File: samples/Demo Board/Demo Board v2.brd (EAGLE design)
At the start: 88.9 x 50.8 mm, 145 parts

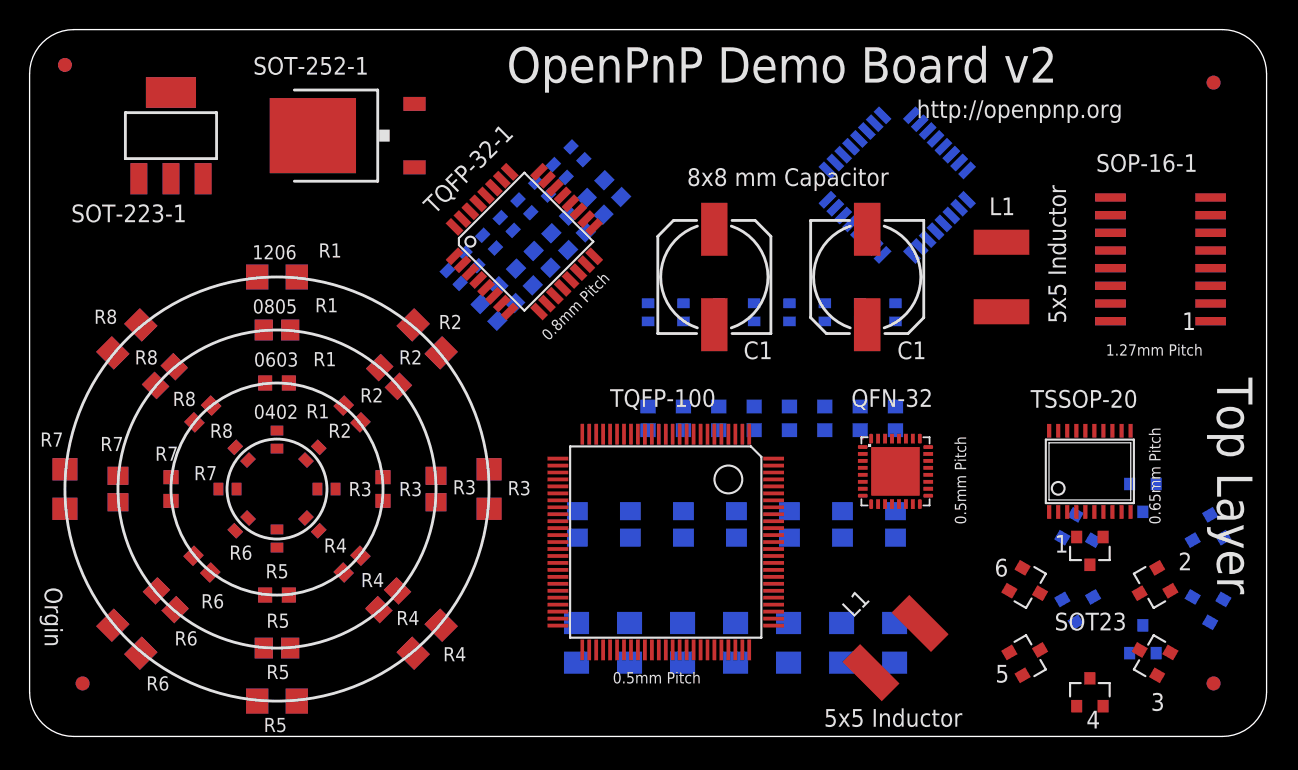
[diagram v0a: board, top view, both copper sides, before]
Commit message: Added coverage for all major IC pitch types. 1mm keepout around all fiducials. Bottom layer tests. Logical placement and labeling for top and bottom layers. Tricky/tall/heavy components (capacitors, inductors). Calibration ruler on bottom layer.
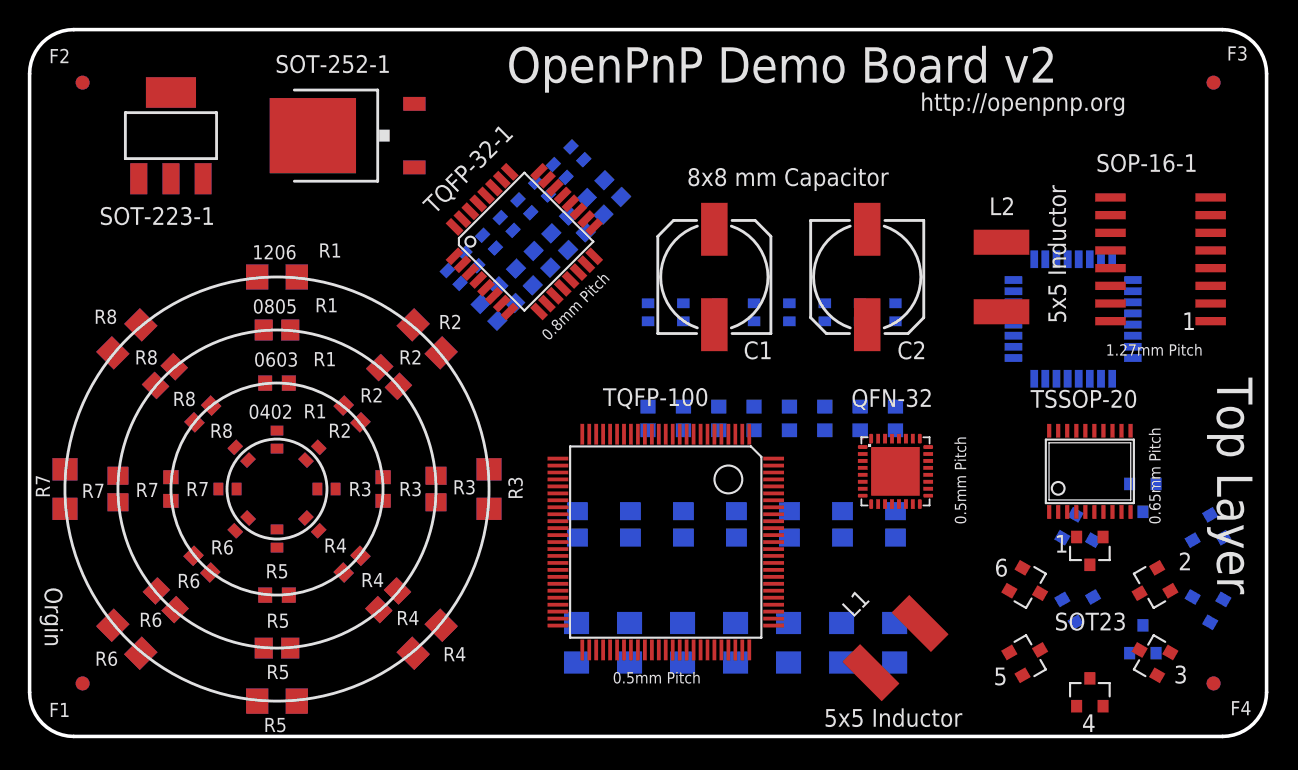
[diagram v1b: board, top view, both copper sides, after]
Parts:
- removed FID-9: (no value), adafruit:FIDUCIAL_1MM
- removed SOP-16-2: (no value), ref-packages:SOP16
- added FID-8: (no value), adafruit:FIDUCIAL_1MM
- moved FID-6 92.0 mm to (3.81, 47.0), flipped to the bottom
- moved FID-3 82.6 mm to (85.1, 47.0)
- moved FID-2 81.3 mm to (3.81, 47.0)
- moved FID-5 44.5 mm to (3.81, 3.81)
- moved TQFP-32-2 15.9 mm to (75.0, 30.0), turned to 0 degrees
- flipped FID-4 to the top
- renumbered FID-14 to FID-7, TQFP-1 to TQFP-32-1
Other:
- board text added: "10x10mm"
- board text added: "1mm Ruler"
- board text added: "C2"
- board text added: "F1"
- board text added: "F2"
- board text added: "F3"
- board text added: "F4"
- board text added: "F5"
- board text added: "F6"
- board text added: "F7"
- board text added: "F8"
- board text added: "L2"
- board text removed: "Bottom Layer"
- board text removed: "SOP-16-2"

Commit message: Add lines to ruler for clarity and to aid in measuring image distortion
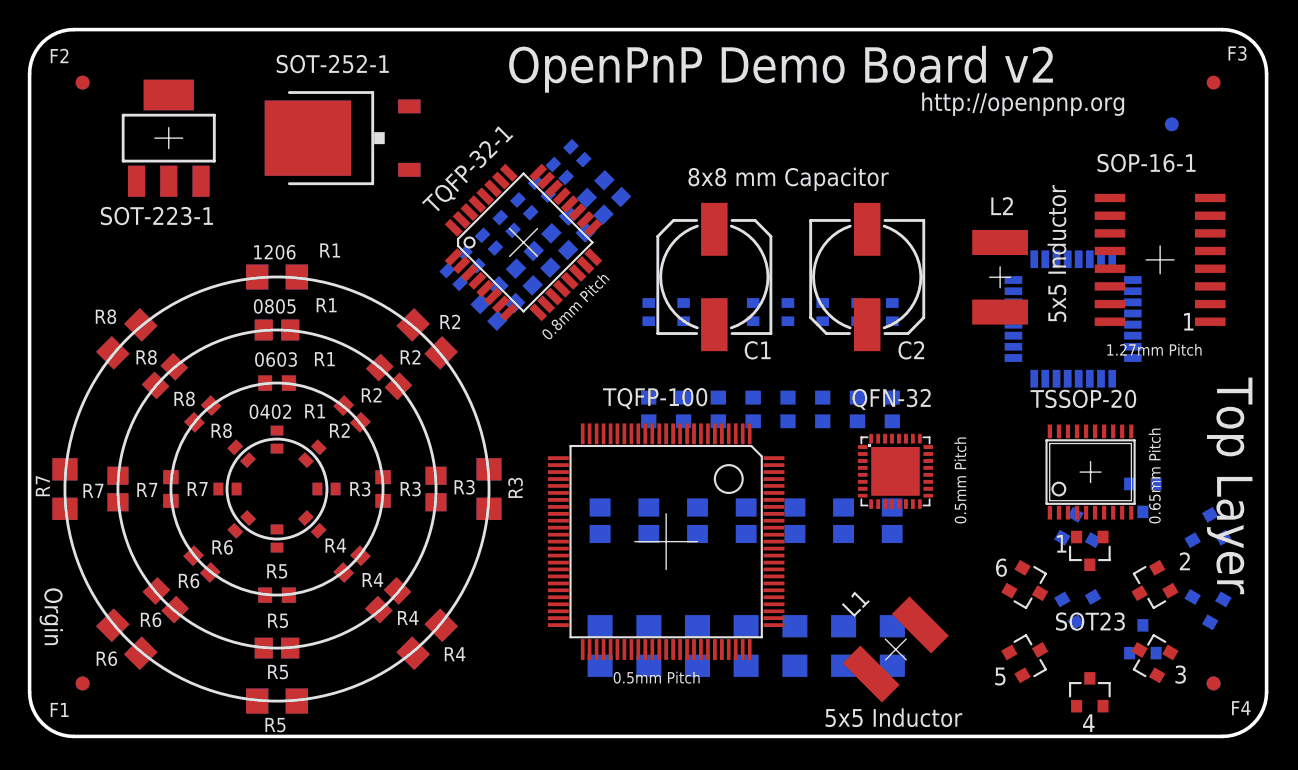
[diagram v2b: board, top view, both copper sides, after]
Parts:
- moved FID-7 4.24 mm to (82.1, 44.0)
- moved R1206-17 1.71 mm to (41.0, 6.50)
- moved R0805-17 1.65 mm to (41.0, 15.5)
- moved R1206-18 1.40 mm to (44.5, 6.50)
- moved R0805-18 1.35 mm to (44.5, 15.5)
- moved R1206-19 1.10 mm to (48.0, 6.50)
- moved R0805-19 1.04 mm to (48.0, 15.5)
- moved R1206-20 0.80 mm to (51.5, 6.50)
- moved R0805-20 0.75 mm to (51.5, 15.5)
- moved R0603-32 0.68 mm to (62.0, 23.5)
- moved R0603-31 0.67 mm to (59.5, 23.5)
- moved R0603-30 0.66 mm to (57.0, 23.5)
- moved R0603-29 0.65 mm to (54.5, 23.5)
- moved R0603-28 0.64 mm to (52.0, 23.5)
- moved R0603-25 0.64 mm to (44.5, 23.5)
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
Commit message: Changed ruler to copper Added .5mm spacing to ruler Added ruler to Top Layer so now it is on top and bottom Added 0201 components. Created new components named BOTTOM_RULER_ORIGIN and TOP_RULER_ORIGIN. Now they will show up in job list so you can zoom to them.
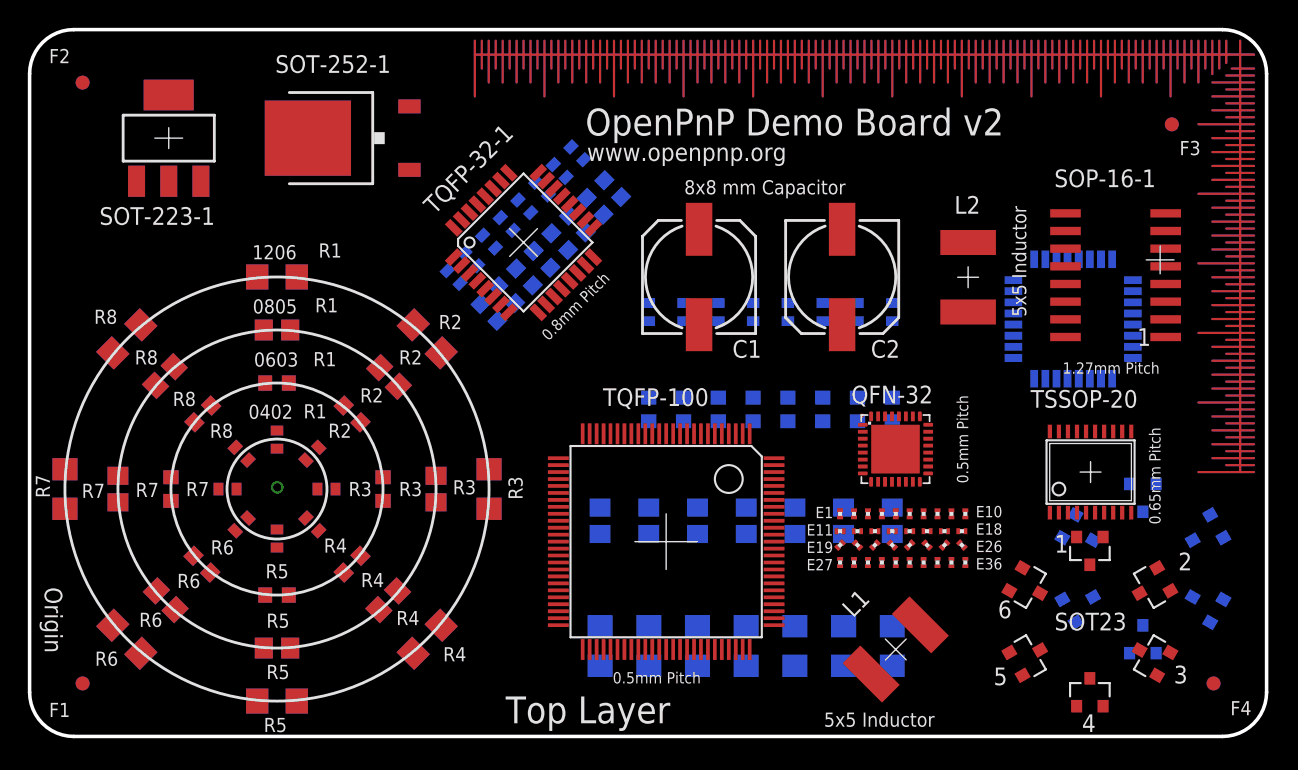
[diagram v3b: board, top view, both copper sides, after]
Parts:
- added BOTTOM_RULER_ORGIN, BOTTOM_RULER_ORGIN1: (no value), ref-packages:REFERENCE_BOTTOM
- added E$12, E$13, E$14, E$15, E$16, E$17, E$19, E$2, E$20, E$21, E$22, E$23, E$24, E$25, E$26, E$28, E$29, E$3, E$30, E$31, E$32, E$33, E$34, E$35, E$4, E$5, E$6, E$7, E$8, E$9, E1, E10, E11, E18, E27, E36: (no value), rcl:R0201
- moved FID-3 4.24 mm to (82.1, 44.0)
- moved SOP-16-1 3.38 mm to (78.0, 33.1)
- moved L2 2.30 mm to (67.5, 33.0)
- moved C2 1.80 mm to (58.4, 33.0)
- moved QFN-32 1.60 mm to (62.2, 20.6)
- moved C1 1.10 mm to (48.1, 33.0)
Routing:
- net S$1: track 0.00 -> 60.0 mm
- net S$288: track 0.00 -> 55.9 mm
- net S$240: track 0.00 -> 35.0 mm
- net S$78: track 0.00 -> 34.9 mm
- net S$98: track 0.00 -> 6.00 mm
- net S$97: track 0.00 -> 6.00 mm
- net S$91: track 0.00 -> 6.00 mm
- net S$90: track 0.00 -> 6.00 mm
- net S$84: track 0.00 -> 6.00 mm
- net S$83: track 0.00 -> 6.00 mm
- net S$70: track 0.00 -> 6.00 mm
- net S$69: track 0.00 -> 6.00 mm
- net S$63: track 0.00 -> 6.00 mm
- net S$62: track 0.00 -> 6.00 mm
- net S$6: track 0.00 -> 6.00 mm
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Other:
- board text added: "0.5, 1, 5, 10 mm"
- board text added: "E1"
- board text added: "E10"
- board text added: "E11"
- board text added: "E18"
- board text added: "E19"
- board text added: "E26"
- board text added: "E27"
- board text added: "E36"
- board text added: "Origin"
- board text added: "Ruler Spacing"
- board text added: "www.openpnp.org"
- board text removed: "1mm Ruler"
- board text removed: "Orgin"
- board text removed: "http://openpnp.org"

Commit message: Changing the sample to the version i physically have
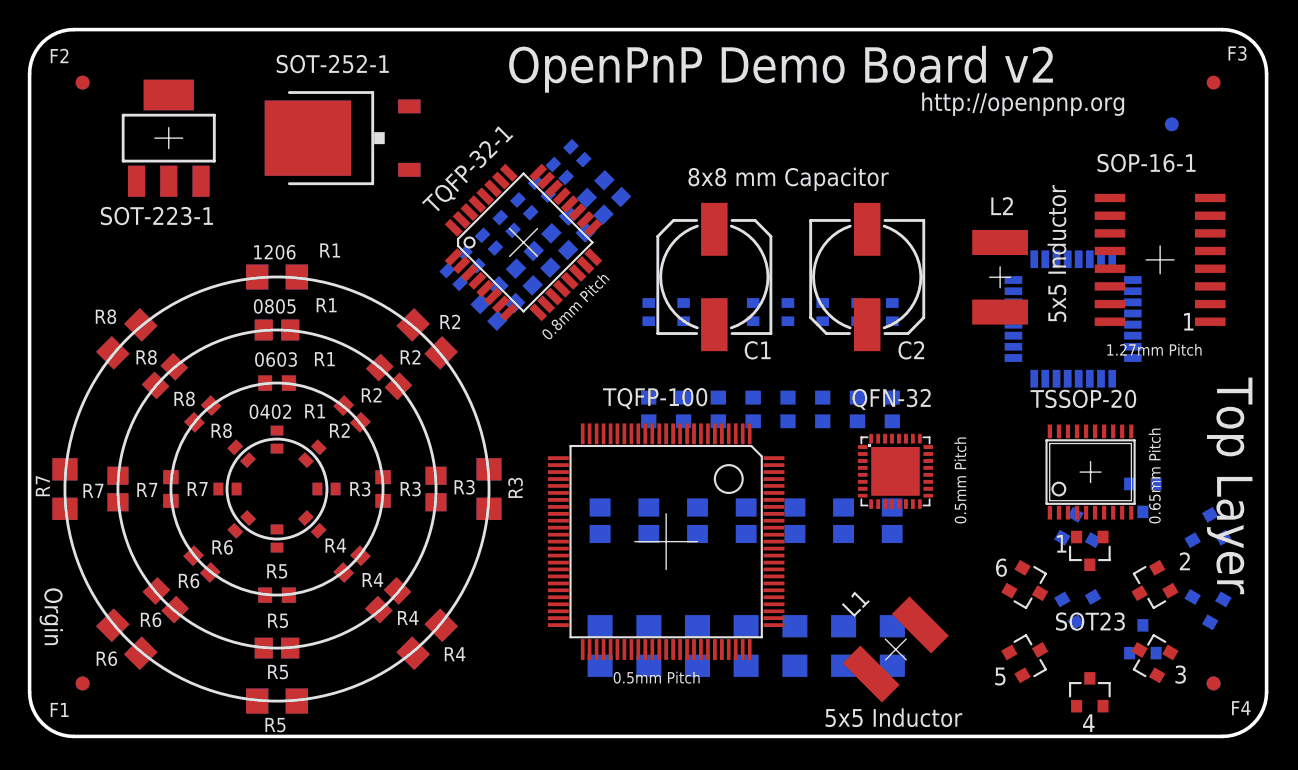
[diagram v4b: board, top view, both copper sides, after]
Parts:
- removed BOTTOM_RULER_ORGIN, BOTTOM_RULER_ORGIN1: (no value), ref-packages:REFERENCE_BOTTOM
- removed E$12, E$13, E$14, E$15, E$16, E$17, E$19, E$2, E$20, E$21, E$22, E$23, E$24, E$25, E$26, E$28, E$29, E$3, E$30, E$31, E$32, E$33, E$34, E$35, E$4, E$5, E$6, E$7, E$8, E$9, E1, E10, E11, E18, E27, E36: (no value), rcl:R0201
- moved FID-3 4.24 mm to (85.1, 47.0)
- moved SOP-16-1 3.38 mm to (81.2, 34.2)
- moved L2 2.30 mm to (69.8, 33.0)
- moved C2 1.80 mm to (60.2, 33.0)
- moved QFN-32 1.60 mm to (62.2, 19.1)
- moved C1 1.10 mm to (49.2, 33.0)
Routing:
- net S$1: track 60.0 -> 0.00 mm
- net S$288: track 55.9 -> 0.00 mm
- net S$240: track 35.0 -> 0.00 mm
- net S$78: track 34.9 -> 0.00 mm
- net S$98: track 6.00 -> 0.00 mm
- net S$97: track 6.00 -> 0.00 mm
- net S$91: track 6.00 -> 0.00 mm
- net S$90: track 6.00 -> 0.00 mm
- net S$84: track 6.00 -> 0.00 mm
- net S$83: track 6.00 -> 0.00 mm
- net S$70: track 6.00 -> 0.00 mm
- net S$69: track 6.00 -> 0.00 mm
- net S$63: track 6.00 -> 0.00 mm
- net S$62: track 6.00 -> 0.00 mm
- net S$6: track 6.00 -> 0.00 mm
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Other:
- board text added: "1mm Ruler"
- board text added: "Orgin"
- board text added: "http://openpnp.org"
- board text removed: "0.5, 1, 5, 10 mm"
- board text removed: "E1"
- board text removed: "E10"
- board text removed: "E11"
- board text removed: "E18"
- board text removed: "E19"
- board text removed: "E26"
- board text removed: "E27"
- board text removed: "E36"
- board text removed: "Origin"
- board text removed: "Ruler Spacing"
- board text removed: "www.openpnp.org"
